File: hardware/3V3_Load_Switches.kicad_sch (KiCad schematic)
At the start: 28 parts, among them Q18 SI2302DDS-T1-GE3, Q19 SI2302DDS-T1-GE3, Q20 SI2302DDS-T1-GE3, U1 LMV321RIYLT, U2 INA199C3DCKR, U3 INA199C3DCKR, U4 INA199C1DCKR, U5 NVTFS5116PLTAG, U6 NVTFS5116PLTAG, U7 NVTFS5116PLTAG

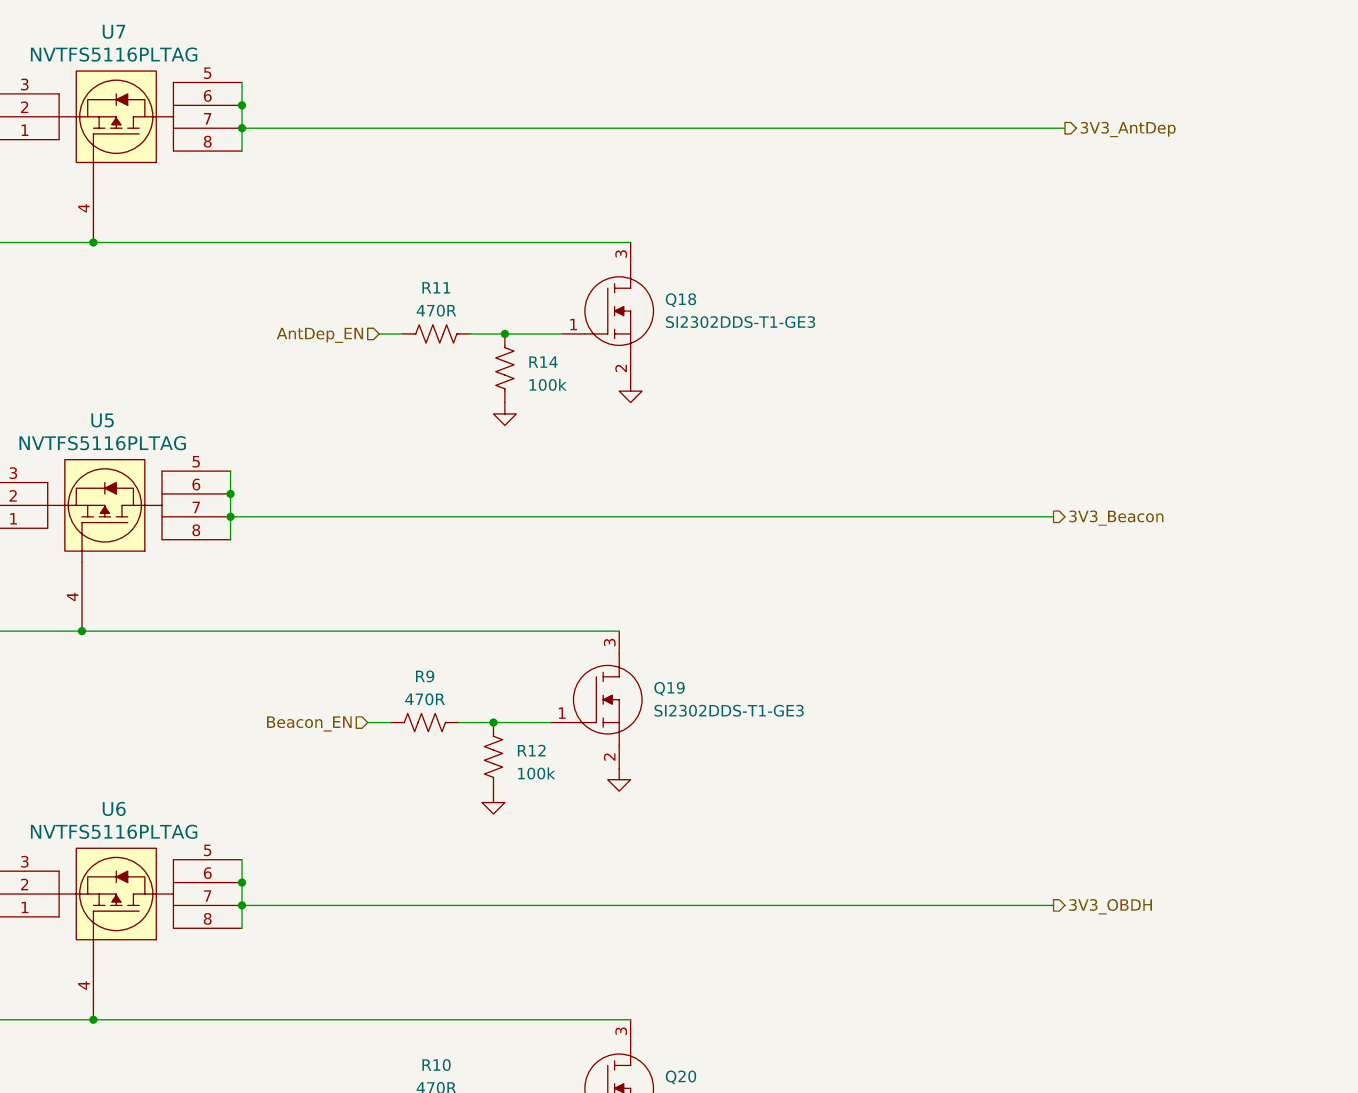
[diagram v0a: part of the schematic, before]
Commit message: hardware: Adding some 3D models, changing the placement of components and routing more nets.
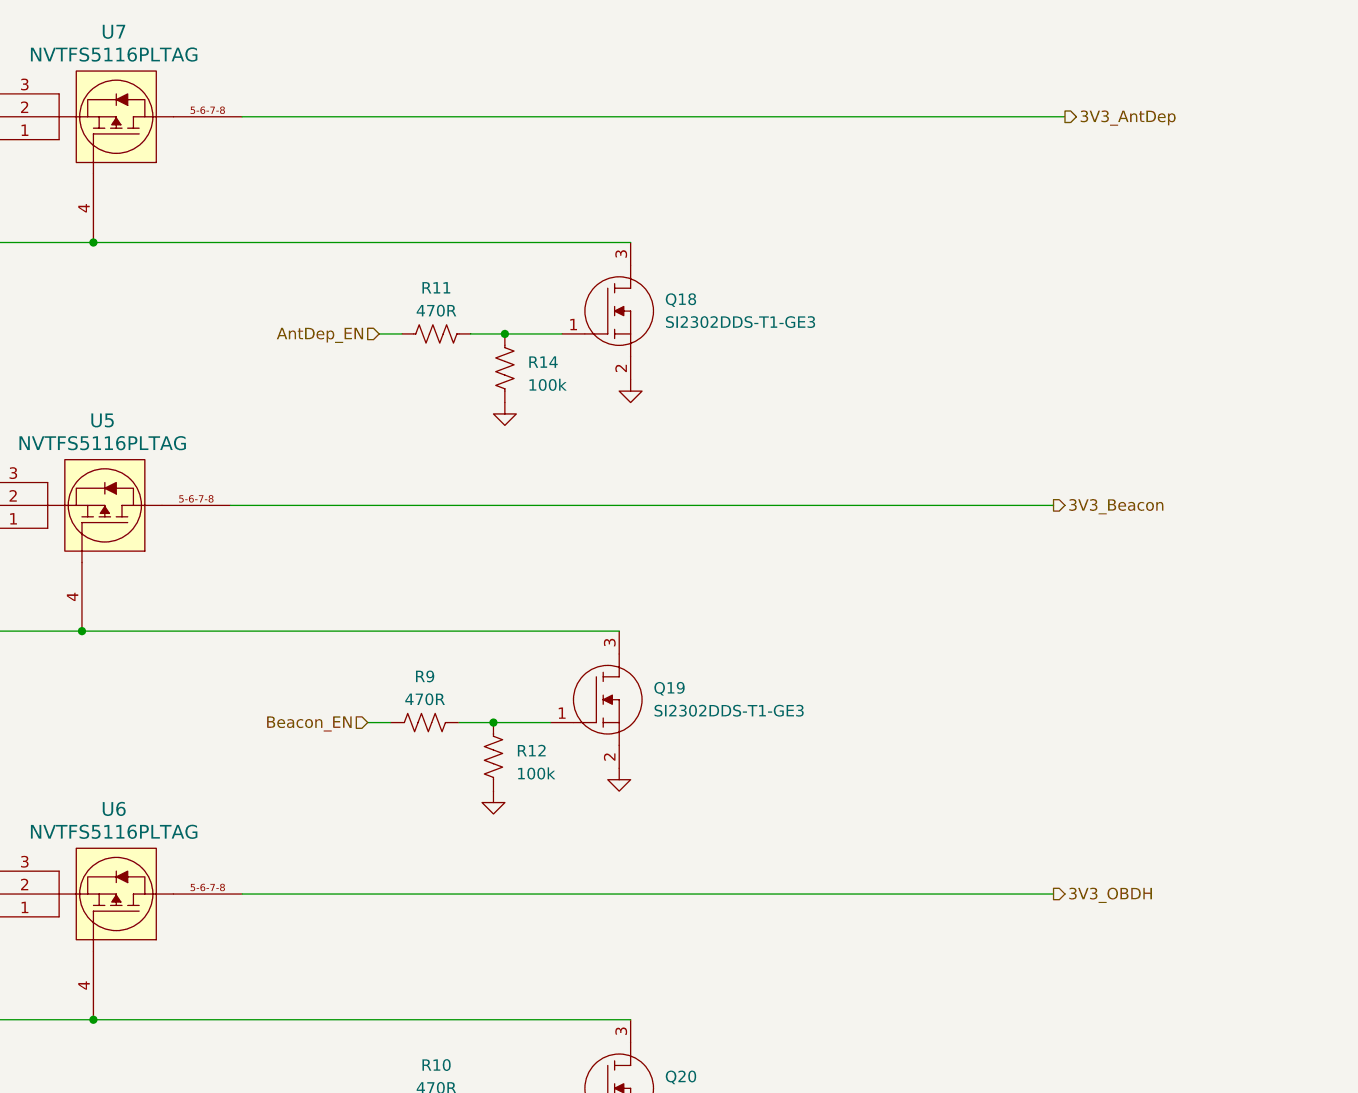
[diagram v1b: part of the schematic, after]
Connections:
- net 3V3_AntDep: now also U7.5-6-7-8; no longer U7.5, U7.6, U7.7, U7.8
- net 3V3_Beacon: now also U5.5-6-7-8; no longer U5.5, U5.6, U5.7, U5.8
- net 3V3_OBDH: now also U6.5-6-7-8; no longer U6.5, U6.6, U6.7, U6.8
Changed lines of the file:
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@@
   (junction (at 121.92 29.21) (diameter 0) (color 0 0 0 0)
   )
-  (junction (at 148.59 71.12) (diameter 0) (color 0 0 0 0)
-  )
   (junction (at 76.2 29.21) (diameter 0) (color 0 0 0 0)
   )
   (junction (at 76.2 72.39) (diameter 0) (color 0 0 0 0)
   )
-  (junction (at 148.59 73.66) (diameter 0) (color 0 0 0 0)
-  )
   (junction (at 57.15 93.98) (diameter 0) (color 0 0 0 0)
   )
@@
   (junction (at 177.8 96.52) (diameter 0) (color 0 0 0 0)
   )
-  (junction (at 149.86 116.84) (diameter 0) (color 0 0 0 0)
-  )
   (junction (at 66.04 142.24) (diameter 0) (color 0 0 0 0)
   )
   (junction (at 57.15 137.16) (diameter 0) (color 0 0 0 0)
   )
-  (junction (at 149.86 27.94) (diameter 0) (color 0 0 0 0)
-  )
-  (junction (at 149.86 114.3) (diameter 0) (color 0 0 0 0)
-  )
-  (junction (at 149.86 30.48) (diameter 0) (color 0 0 0 0)
-  )
   (junction (at 133.35 129.54) (diameter 0) (color 0 0 0 0)
   )
@@
     (stroke (width 0) (type default))
   )
-  (wire (pts (xy 149.86 116.84) (xy 149.86 119.38))
-    (stroke (width 0) (type default))
-  )
   (wire (pts (xy 175.26 139.7) (xy 179.07 139.7))
     (stroke (width 0) (type default))
@@
     (stroke (width 0) (type default))
   )
-  (wire (pts (xy 149.86 27.94) (xy 149.86 30.48))
-    (stroke (width 0) (type default))
-  )
   (wire (pts (xy 104.14 86.36) (xy 132.08 86.36))
     (stroke (width 0) (type default))
@@
   )
   (wire (pts (xy 256.54 151.13) (xy 248.92 151.13))
-    (stroke (width 0) (type default))
-  )
-  (wire (pts (xy 148.59 73.66) (xy 148.59 76.2))
     (stroke (width 0) (type default))
   )
@@
     (stroke (width 0) (type default))
   )
-  (wire (pts (xy 149.86 111.76) (xy 149.86 114.3))
-    (stroke (width 0) (type default))
-  )
   (wire (pts (xy 104.14 72.39) (xy 120.65 72.39))
     (stroke (width 0) (type default))
@@
     (stroke (width 0) (type default))
   )
-  (wire (pts (xy 148.59 71.12) (xy 148.59 73.66))
-    (stroke (width 0) (type default))
-  )
-  (wire (pts (xy 149.86 30.48) (xy 241.3 30.48))
-    (stroke (width 0) (type default))
-  )
-  (wire (pts (xy 149.86 116.84) (xy 240.03 116.84))
+  (wire (pts (xy 149.86 29.21) (xy 241.3 29.21))
+    (stroke (width 0) (type default))
+  )
+  (wire (pts (xy 149.86 115.57) (xy 240.03 115.57))
     (stroke (width 0) (type default))
   )
@@
   )
   (wire (pts (xy 57.15 115.57) (xy 63.5 115.57))
-    (stroke (width 0) (type default))
-  )
-  (wire (pts (xy 149.86 25.4) (xy 149.86 27.94))
     (stroke (width 0) (type default))
   )
@@
     (stroke (width 0) (type default))
   )
-  (wire (pts (xy 148.59 73.66) (xy 240.03 73.66))
+  (wire (pts (xy 148.59 72.39) (xy 240.03 72.39))
     (stroke (width 0) (type default))
   )
@@
   )
   (wire (pts (xy 105.41 29.21) (xy 105.41 35.56))
-    (stroke (width 0) (type default))
-  )
-  (wire (pts (xy 148.59 68.58) (xy 148.59 71.12))
     (stroke (width 0) (type default))
   )
@@
     (stroke (width 0) (type default))
   )
-  (wire (pts (xy 149.86 114.3) (xy 149.86 116.84))
-    (stroke (width 0) (type default))
-  )
   (wire (pts (xy 71.12 72.39) (xy 76.2 72.39))
-    (stroke (width 0) (type default))
-  )
-  (wire (pts (xy 149.86 30.48) (xy 149.86 33.02))
     (stroke (width 0) (type default))
   )
@@
     (effects (font (size 1.27 1.27)) (justify right bottom))
   )
-  (hierarchical_label "3V3_Beacon" (shape output) (at 240.03 73.66 0) (fields_autoplaced)
+  (hierarchical_label "3V3_Beacon" (shape output) (at 240.03 72.39 0) (fields_autoplaced)
     (effects (font (size 1.27 1.27)) (justify left))
   )
@@
     (effects (font (size 1.27 1.27)) (justify right))
   )
-  (hierarchical_label "3V3_OBDH" (shape output) (at 240.03 116.84 0) (fields_autoplaced)
+  (hierarchical_label "3V3_OBDH" (shape output) (at 240.03 115.57 0) (fields_autoplaced)
     (effects (font (size 1.27 1.27)) (justify left))
   )
@@
     (effects (font (size 1.27 1.27)) (justify right))
   )
-  (hierarchical_label "3V3_AntDep" (shape output) (at 241.3 30.48 0) (fields_autoplaced)
+  (hierarchical_label "3V3_AntDep" (shape output) (at 241.3 29.21 0) (fields_autoplaced)
     (effects (font (size 1.27 1.27)) (justify left))
   )
@@
     (pin "3")
     (pin "4")
-    (pin "5")
-    (pin "6")
-    (pin "7")
-    (pin "8")
+    (pin "5-6-7-8")
     (instances
       (project "eps-re_project"
@@
     (pin "3")
     (pin "4")
-    (pin "5")
-    (pin "6")
-    (pin "7")
-    (pin "8")
+    (pin "5-6-7-8")
     (instances
       (project "eps-re_project"
@@
     (pin "3")
     (pin "4")
-    (pin "5")
-    (pin "6")
-    (pin "7")
-    (pin "8")
-    (instances
-      (project "eps-re_project"
+    (pin "5-6-7-8")
+    (instances
+      (project "eps-re_project"

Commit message: hardware: Updating schematics and layout.
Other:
- note added: "Output current ≤ 2A"
- note added: "Output current ≤ 300mA"
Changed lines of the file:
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@@
     (date "2023-08-03")
     (rev "v0.0")
-    (comment 1 "João C. E. Barcellos <joaoclaudiobarcellos@gmail.com>")
-    (comment 2 "Laura Debastiani <laudebastiani@gmail.com>")
+    (comment 1 "Davi Figueiredo <figueiredo.davi7@gmail.com> ")
+    (comment 2 "João C. E. Barcellos <joaoclaudiobarcellos@gmail.com>")
+    (comment 3 "Laura Debastiani <laudebastiani@gmail.com>")
   )
   (junction (at 133.35 43.18) (diameter 0) (color 0 0 0 0)
@@
   )
   (wire (pts (xy 105.41 29.21) (xy 121.92 29.21))
-    (stroke (width 0) (type default))
+    (stroke (width 1) (type default))
   )
   (wire (pts (xy 76.2 29.21) (xy 76.2 39.37))
@@
   )
   (wire (pts (xy 104.14 72.39) (xy 120.65 72.39))
-    (stroke (width 0) (type default))
+    (stroke (width 1) (type default))
   )
   (wire (pts (xy 167.64 53.34) (xy 165.1 53.34))
@@
   )
   (wire (pts (xy 57.15 72.39) (xy 63.5 72.39))
-    (stroke (width 0) (type default))
+    (stroke (width 1) (type default))
   )
   (wire (pts (xy 121.92 29.21) (xy 121.92 31.75))
-    (stroke (width 0) (type default))
+    (stroke (width 1) (type default))
   )
   (wire (pts (xy 66.04 142.24) (xy 76.2 142.24))
@@
   )
   (wire (pts (xy 76.2 72.39) (xy 104.14 72.39))
-    (stroke (width 0) (type default))
+    (stroke (width 1) (type default))
   )
   (wire (pts (xy 121.92 113.03) (xy 121.92 115.57))
-    (stroke (width 0) (type default))
+    (stroke (width 1) (type default))
   )
   (wire (pts (xy 173.99 96.52) (xy 177.8 96.52))
@@
   )
   (wire (pts (xy 149.86 29.21) (xy 241.3 29.21))
-    (stroke (width 0) (type default))
+    (stroke (width 1) (type default))
   )
   (wire (pts (xy 149.86 115.57) (xy 240.03 115.57))
-    (stroke (width 0) (type default))
+    (stroke (width 1) (type default))
   )
   (wire (pts (xy 66.04 99.06) (xy 57.15 99.06))
@@
   )
   (wire (pts (xy 121.92 115.57) (xy 121.92 118.11))
-    (stroke (width 0) (type default))
+    (stroke (width 1) (type default))
   )
   (wire (pts (xy 76.2 72.39) (xy 76.2 82.55))
@@
   )
   (wire (pts (xy 22.86 72.39) (xy 22.86 115.57))
-    (stroke (width 0) (type default))
+    (stroke (width 1) (type default))
   )
   (wire (pts (xy 104.14 72.39) (xy 104.14 78.74))
@@
   )
   (wire (pts (xy 22.86 72.39) (xy 57.15 72.39))
-    (stroke (width 0) (type default))
+    (stroke (width 1) (type default))
   )
   (wire (pts (xy 71.12 29.21) (xy 76.2 29.21))
-    (stroke (width 0) (type default))
+    (stroke (width 1) (type default))
   )
   (wire (pts (xy 22.86 115.57) (xy 57.15 115.57))
-    (stroke (width 0) (type default))
+    (stroke (width 1) (type default))
   )
   (wire (pts (xy 105.41 129.54) (xy 133.35 129.54))
@@
   )
   (wire (pts (xy 71.12 115.57) (xy 76.2 115.57))
-    (stroke (width 0) (type default))
+    (stroke (width 1) (type default))
   )
   (wire (pts (xy 81.28 172.72) (xy 81.28 180.34))
@@
   )
   (wire (pts (xy 76.2 115.57) (xy 105.41 115.57))
-    (stroke (width 0) (type default))
+    (stroke (width 1) (type default))
   )
   (wire (pts (xy 22.86 163.83) (xy 22.86 168.91))
@@
   )
   (wire (pts (xy 76.2 29.21) (xy 105.41 29.21))
-    (stroke (width 0) (type default))
+    (stroke (width 1) (type default))
   )
   (wire (pts (xy 120.65 72.39) (xy 120.65 74.93))
-    (stroke (width 0) (type default))
+    (stroke (width 1) (type default))
   )
   (wire (pts (xy 57.15 115.57) (xy 63.5 115.57))
-    (stroke (width 0) (type default))
+    (stroke (width 1) (type default))
   )
   (wire (pts (xy 105.41 43.18) (xy 133.35 43.18))
@@
   )
   (wire (pts (xy 121.92 26.67) (xy 121.92 29.21))
-    (stroke (width 0) (type default))
+    (stroke (width 1) (type default))
   )
   (wire (pts (xy 22.86 29.21) (xy 22.86 72.39))
-    (stroke (width 0) (type default))
+    (stroke (width 1) (type default))
   )
   (wire (pts (xy 81.28 163.83) (xy 81.28 167.64))
@@
   )
   (wire (pts (xy 105.41 115.57) (xy 121.92 115.57))
-    (stroke (width 0) (type default))
+    (stroke (width 1) (type default))
   )
   (wire (pts (xy 66.04 55.88) (xy 76.2 55.88))
@@
   )
   (wire (pts (xy 22.86 29.21) (xy 57.15 29.21))
-    (stroke (width 0) (type default))
+    (stroke (width 1) (type default))
   )
   (wire (pts (xy 57.15 39.37) (xy 57.15 43.18))
@@
   )
   (wire (pts (xy 22.86 29.21) (xy 19.05 29.21))
-    (stroke (width 0) (type default))
+    (stroke (width 1) (type default))
   )
   (wire (pts (xy 57.15 125.73) (xy 57.15 129.54))
@@
   )
   (wire (pts (xy 148.59 72.39) (xy 240.03 72.39))
-    (stroke (width 0) (type default))
+    (stroke (width 1) (type default))
   )
   (wire (pts (xy 57.15 29.21) (xy 57.15 39.37))
@@
   )
   (wire (pts (xy 120.65 69.85) (xy 120.65 72.39))
-    (stroke (width 0) (type default))
+    (stroke (width 1) (type default))
   )
   (wire (pts (xy 177.8 96.52) (xy 184.15 96.52))
@@
   )
   (wire (pts (xy 57.15 29.21) (xy 63.5 29.21))
-    (stroke (width 0) (type default))
+    (stroke (width 1) (type default))
   )
   (wire (pts (xy 71.12 72.39) (xy 76.2 72.39))
-    (stroke (width 0) (type default))
+    (stroke (width 1) (type default))
   )
   (wire (pts (xy 22.86 115.57) (xy 22.86 156.21))
@@
     (stroke (width 0) (type default))
   )
+  (text "Output current ≤ 300mA" (at 204.47 114.3 0)
+    (effects (font (size 1.27 1.27)) (justify left bottom))
+  )
+  (text "Output current ≤ 300mA" (at 204.47 71.12 0)
+    (effects (font (size 1.27 1.27)) (justify left bottom))
+  )
+  (text "Output current ≤ 2A" (at 204.47 27.94 0)
+    (effects (font (size 1.27 1.27)) (justify left bottom))
+  )
   (label "AMUX15" (at 248.92 143.51 180) (fields_autoplaced)
